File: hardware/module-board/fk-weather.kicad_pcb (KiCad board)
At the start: 2 copper layers, 37.5 x 103 mm, 72 parts, among them J1 MICRO-USB, J10 CONN_01x06, J11 CONN_01x06, J2 CONN_01x05, J3 CONN_01x03_SERIAL, J4 CONN_01x04, J5 Conn_01x02, J6 CONN_02x05_SWD, J7 CONN_01x05, Q4 2N7002LT1G, SW1 SPNO, U1 ATSAMD21G18A-AU, U2 MCP1700T-3302E/MB, U3 TPS2051B, U4 S25FL116K0XMFI041, U5 SK6812, U6 PCF8523, Y1 FC-135, Y2 FC-135

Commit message: Adding some pull downs.
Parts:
- added R3: ?, conservify:RES-0603, F.Cu at (94.0, 143.4)
- added R5: ?, conservify:RES-0603, F.Cu at (88.4, 146.2)
- J5: value Conn_01x02 -> CONN_01x02
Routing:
- net /D8_PERIPH_EN: track 27.7 -> 30.4 mm, vias 2 -> 3
- net /PERIPH_3V3: track 24.3 -> 26.2 mm
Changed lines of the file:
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@@
-(kicad_pcb (version 20171130) (host pcbnew 5.0.0-fee4fd1~66~ubuntu16.04.1)
+(kicad_pcb (version 20171130) (host pcbnew 5.0.1-33cea8e~67~ubuntu18.04.1)
   (general
     (thickness 1.6)
     (drawings 16)
-    (tracks 709)
+    (tracks 715)
     (zones 0)
-    (modules 72)
+    (modules 74)
     (nets 80)
   )
@@
     (pad_drill 0)
     (pad_to_mask_clearance 0.1016)
+    (solder_mask_min_width 0.25)
     (pad_to_paste_clearance_ratio -0.05)
     (aux_axis_origin 127 127)
@@
       (effects (font (size 0.8 0.8) (thickness 0.12)))
     )
-    (fp_text value Conn_01x02 (at 0 1.6 90) (layer Eco1.User) hide
+    (fp_text value CONN_01x02 (at 0 1.6 90) (layer Eco1.User) hide
       (effects (font (size 0.6 0.6) (thickness 0.1)))
     )
@@
     (pad "" np_thru_hole circle (at -6 0 270) (size 2.36 2.36) (drill 2.36) (layers *.Cu *.Mask F.SilkS))
   )
+  (module conservify:RES-0603 (layer F.Cu)
+    (at 93.98 143.383 180)
+    (descr "Capacitor SMD 0603")
+    (tags "capacitor 0603")
+    (attr smd)
+    (fp_text reference R3 (at 0 -1.5748 180) (layer F.SilkS) hide
+      (effects (font (size 1 1) (thickness 0.15)))
+    )
+    (fp_text value ? (at 0 1.9 180) (layer F.Fab)
+      (effects (font (size 1 1) (thickness 0.15)))
+    )
+    (fp_line (start -1.65 -0.75) (end -1.65 0.75) (layer F.CrtYd) (width 0.05))
+    (fp_line (start -1.65 0.75) (end 1.65 0.75) (layer F.CrtYd) (width 0.05))
+    (fp_line (start 1.65 0.75) (end 1.65 -0.75) (layer F.CrtYd) (width 0.05))
+    (fp_line (start 1.65 -0.75) (end -1.65 -0.75) (layer F.CrtYd) (width 0.05))
+    (fp_line (start -1.6 -0.7) (end -1.6 0.7) (layer F.SilkS) (width 0.15))
+    (fp_line (start 1.6 -0.7) (end 1.6 0.7) (layer F.SilkS) (width 0.15))
+    (fp_line (start -1.6 -0.7) (end 1.6 -0.7) (layer F.SilkS) (width 0.15))
+    (fp_line (start 1.6 0.7) (end -1.6 0.7) (layer F.SilkS) (width 0.15))
+    (pad 1 smd rect (at -0.85 0 180) (size 1.1 1) (layers F.Cu F.Paste F.Mask)
+      (net 1 GND))
+    (pad 2 smd rect (at 0.85 0 180) (size 1.1 1) (layers F.Cu F.Paste F.Mask)
+      (net 76 /D8_PERIPH_EN))
+  )
+  (module conservify:RES-0603 (layer F.Cu)
+    (at 88.392 146.177)
+    (descr "Capacitor SMD 0603")
+    (tags "capacitor 0603")
+    (attr smd)
+    (fp_text reference R5 (at 0 -1.5748) (layer F.SilkS) hide
+      (effects (font (size 1 1) (thickness 0.15)))
+    )
+    (fp_text value ? (at 0 1.9) (layer F.Fab)
+      (effects (font (size 1 1) (thickness 0.15)))
+    )
+    (fp_line (start 1.6 0.7) (end -1.6 0.7) (layer F.SilkS) (width 0.15))
+    (fp_line (start -1.6 -0.7) (end 1.6 -0.7) (layer F.SilkS) (width 0.15))
+    (fp_line (start 1.6 -0.7) (end 1.6 0.7) (layer F.SilkS) (width 0.15))
+    (fp_line (start -1.6 -0.7) (end -1.6 0.7) (layer F.SilkS) (width 0.15))
+    (fp_line (start 1.65 -0.75) (end -1.65 -0.75) (layer F.CrtYd) (width 0.05))
+    (fp_line (start 1.65 0.75) (end 1.65 -0.75) (layer F.CrtYd) (width 0.05))
+    (fp_line (start -1.65 0.75) (end 1.65 0.75) (layer F.CrtYd) (width 0.05))
+    (fp_line (start -1.65 -0.75) (end -1.65 0.75) (layer F.CrtYd) (width 0.05))
+    (pad 2 smd rect (at 0.85 0) (size 1.1 1) (layers F.Cu F.Paste F.Mask)
+      (net 65 /PERIPH_3V3))
+    (pad 1 smd rect (at -0.85 0) (size 1.1 1) (layers F.Cu F.Paste F.Mask)
+      (net 1 GND))
+  )
   (gr_text SERIAL (at 113.792 159.131 90) (layer F.SilkS)
     (effects (font (size 0.8 0.8) (thickness 0.2)))
@@
   (segment (start 94.471414 148.1963) (end 94.0834 148.1963) (width 0.254) (layer F.Cu) (net 65))
   (segment (start 94.0834 148.1963) (end 92.8294 148.1963) (width 0.254) (layer F.Cu) (net 65))
-  (segment (start 87.5783 147.6765) (end 87.4649 147.7899) (width 0.254) (layer F.Cu) (net 65))
   (segment (start 89.4461 148.1845) (end 87.5783 148.1845) (width 0.254) (layer F.Cu) (net 65))
   (segment (start 92.3176 148.1845) (end 92.3294 148.1963) (width 0.254) (layer F.Cu) (net 65))
   (segment (start 89.4461 148.1845) (end 92.3176 148.1845) (width 0.254) (layer F.Cu) (net 65))
+  (segment (start 89.4461 146.3811) (end 89.242 146.177) (width 0.254) (layer F.Cu) (net 65))
+  (segment (start 89.4461 148.1845) (end 89.4461 146.3811) (width 0.254) (layer F.Cu) (net 65))
   (segment (start 90.814917 139.483979) (end 90.814917 138.422) (width 0.254) (layer F.Cu) (net 66))
   (segment (start 90.814917 138.422) (end 89.806917 137.414) (width 0.254) (layer F.Cu) (net 66))
@@
   (segment (start 92.410919 160.2613) (end 90.5764 160.2613) (width 0.254) (layer F.Cu) (net 76))
   (via (at 90.5764 160.2613) (size 0.5) (drill 0.3) (layers F.Cu B.Cu) (net 76))
+  (segment (start 90.5637 160.274) (end 90.5764 160.2613) (width 0.254) (layer F.Cu) (net 76))
+  (via (at 91.821 143.383) (size 0.5) (drill 0.3) (layers F.Cu B.Cu) (net 76))
+  (segment (start 93.13 143.383) (end 91.821 143.383) (width 0.254) (layer F.Cu) (net 76))
+  (segment (start 90.955353 143.383) (end 90.5764 143.761953) (width 0.254) (layer B.Cu) (net 76))
+  (segment (start 91.821 143.383) (end 90.955353 143.383) (width 0.254) (layer B.Cu) (net 76))
   (segment (start 97.5614 165.9128) (end 97.976358 166.327758) (width 0.254) (layer F.Cu) (net 77))
   (segment (start 97.976358 166.327758) (end 97.976358 167.735929) (width 0.254) (layer F.Cu) (net 77))
@@
     (connect_pads (clearance 0.2032))
     (min_thickness 0.253)
-    (fill (arc_segments 32) (thermal_gap 0.254) (thermal_bridge_width 0.254) (smoothing chamfer))
+    (fill yes (arc_segments 32) (thermal_gap 0.254) (thermal_bridge_width 0.254) (smoothing chamfer))
     (polygon
       (pts
@@
     (connect_pads (clearance 0.2032))
     (min_thickness 0.253)
-    (fill (arc_segments 32) (thermal_gap 0.254) (thermal_bridge_width 0.254) (smoothing chamfer))
+    (fill yes (arc_segments 32) (thermal_gap 0.254) (thermal_bridge_width 0.254) (smoothing chamfer))
     (polygon
       (pts
@@
     (connect_pads (clearance 0.2032))
     (min_thickness 0.253)
-    (fill (arc_segments 32) (thermal_gap 0.254) (thermal_bridge_width 0.254) (smoothing chamfer))
+    (fill yes (arc_segments 32) (thermal_gap 0.254) (thermal_bridge_width 0.254) (smoothing chamfer))
     (polygon
       (pts
@@
     (connect_pads (clearance 0.2032))
     (min_thickness 0.253)
-    (fill (arc_segments 32) (thermal_gap 0.254) (thermal_bridge_width 0.254) (smoothing chamfer))
+    (fill yes (arc_segments 32) (thermal_gap 0.254) (thermal_bridge_width 0.254) (smoothing chamfer))
     (polygon
       (pts

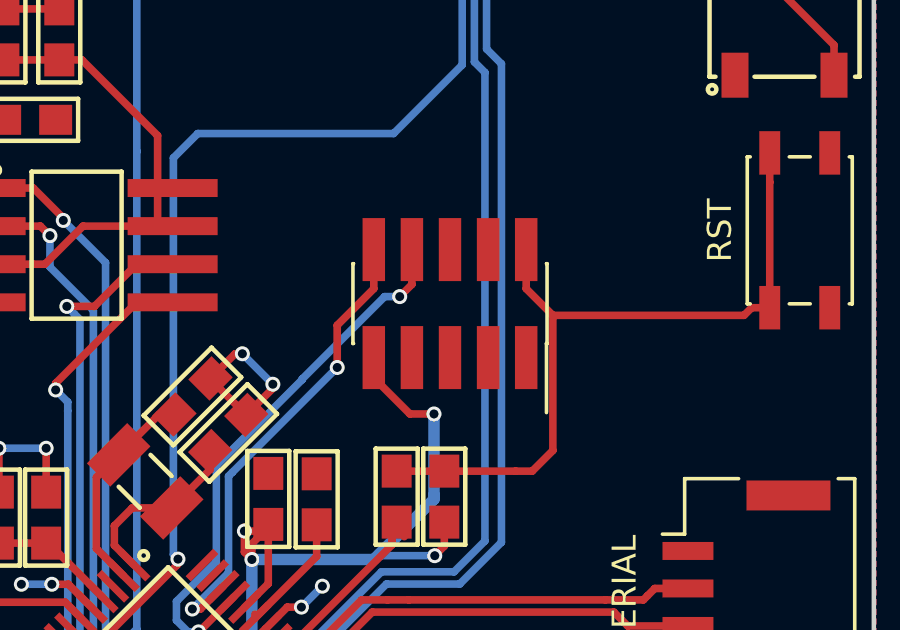
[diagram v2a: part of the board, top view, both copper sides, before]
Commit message: Add orientation indicator to SWD fp.
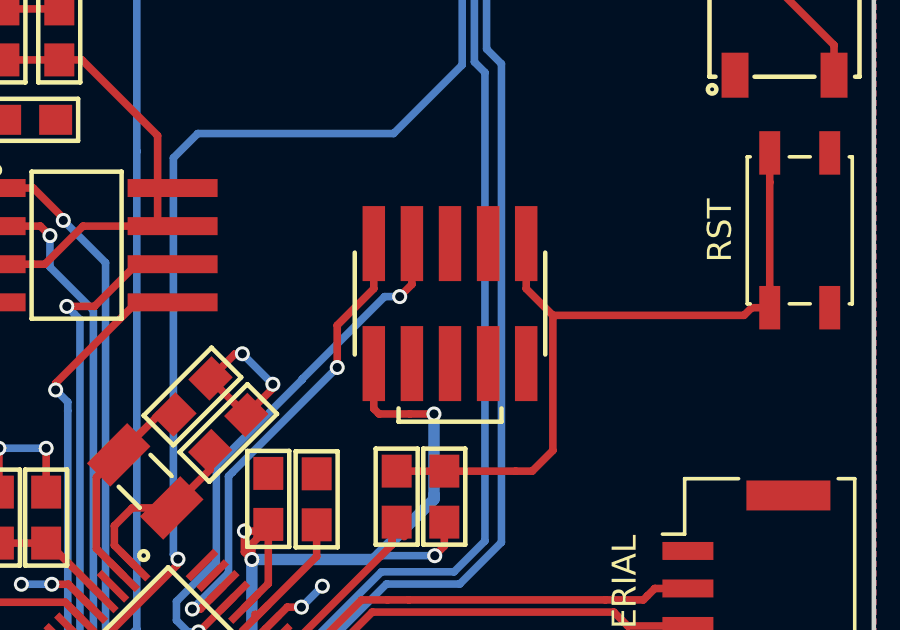
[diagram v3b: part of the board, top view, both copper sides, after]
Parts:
- turned J6 to 0 degrees
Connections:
- J6 pad 1: GND -> 3V3
- J6 pad 10: /SWDIO -> /RST
- J6 pad 2: /RST -> /SWDIO
- J6 pad 3: Net-(J6-Pad3) -> GND
- J6 pad 4: Net-(J6-Pad4) -> /SWCLK
- J6 pad 7: GND -> Net-(J6-Pad7)
- J6 pad 8: /SWCLK -> Net-(J6-Pad8)
- J6 pad 9: 3V3 -> GND
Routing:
- net 3V3: track 290.4 -> 291.5 mm

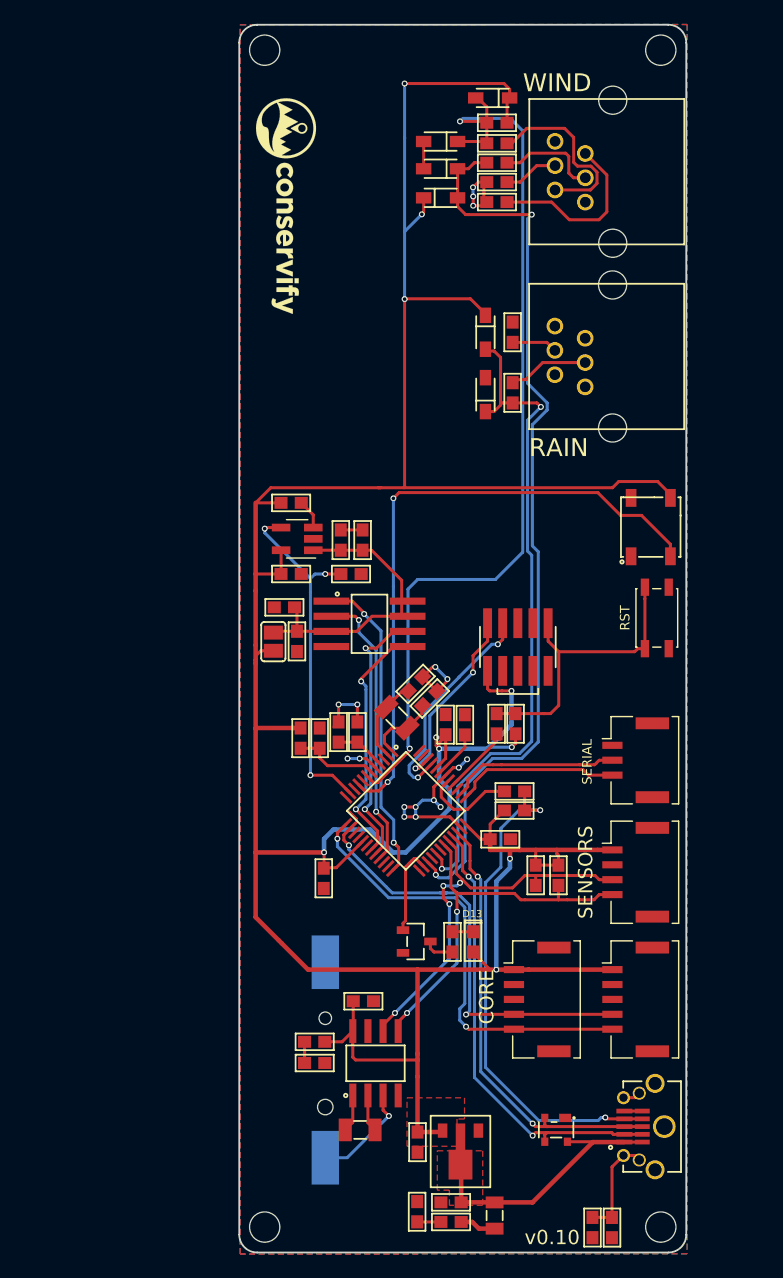
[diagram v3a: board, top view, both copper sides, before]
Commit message: Switch to 2.7mm mounting holes.
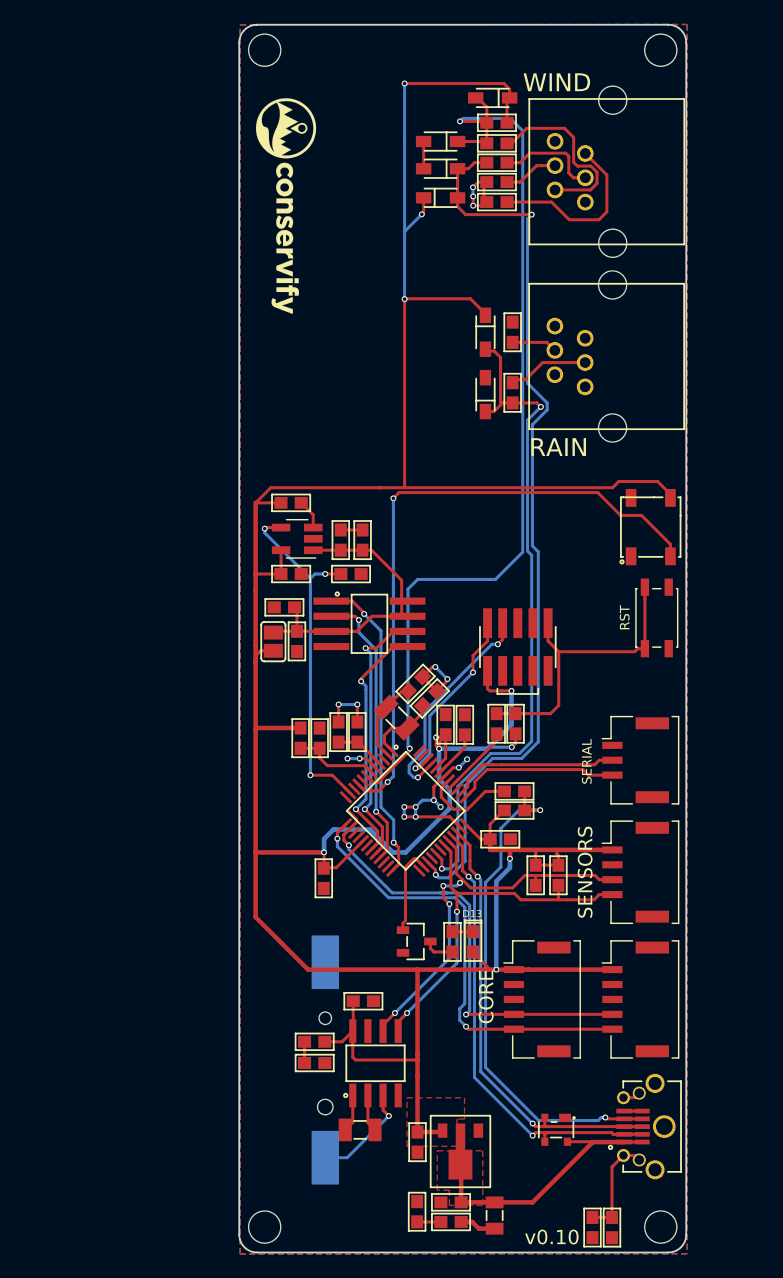
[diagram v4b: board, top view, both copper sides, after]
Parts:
- removed REF** (x4): HOLE_NPTH_2.54MM, conservify:HOLE_NPTH_2.54MM
- added M1: MOUNT_HOLE, conservify:HOLE_NPTH_2.7MM, F.Cu at (86.7, 99.4)
- added M2: MOUNT_HOLE, conservify:HOLE_NPTH_2.7MM, F.Cu at (86.7, 198.2)
- added M3: MOUNT_HOLE, conservify:HOLE_NPTH_2.7MM, F.Cu at (120.0, 198.2)
- added M4: MOUNT_HOLE, conservify:HOLE_NPTH_2.7MM, F.Cu at (120.0, 99.4)
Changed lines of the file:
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@@
     )
-  )
-  (module conservify:HOLE_NPTH_2.54MM (layer F.Cu)
-    (at 86.738445 99.437083 90)
-    (fp_text reference REF** (at 0 -2.54 90) (layer F.SilkS) hide
-      (effects (font (size 1 1) (thickness 0.15)))
-    )
-    (fp_text value HOLE_NPTH_2.54MM (at 0 2.54 90) (layer F.Fab) hide
-      (effects (font (size 1 1) (thickness 0.15)))
-    )
-    (pad "" np_thru_hole circle (at 0 0 90) (size 2.54 2.54) (drill 2.54) (layers *.Cu *.Mask F.SilkS))
-  )
-  (module conservify:HOLE_NPTH_2.54MM (layer F.Cu)
-    (at 86.738445 198.167083 90)
-    (fp_text reference REF** (at 0 -2.54 90) (layer F.SilkS) hide
-      (effects (font (size 1 1) (thickness 0.15)))
-    )
-    (fp_text value HOLE_NPTH_2.54MM (at 0 2.54 90) (layer F.Fab) hide
-      (effects (font (size 1 1) (thickness 0.15)))
-    )
-    (pad "" np_thru_hole circle (at 0 0 90) (size 2.54 2.54) (drill 2.54) (layers *.Cu *.Mask F.SilkS))
-  )
-  (module conservify:HOLE_NPTH_2.54MM (layer F.Cu)
-    (at 119.968445 198.167083 90)
-    (fp_text reference REF** (at 0 -2.54 90) (layer F.SilkS) hide
-      (effects (font (size 1 1) (thickness 0.15)))
-    )
-    (fp_text value HOLE_NPTH_2.54MM (at 0 2.54 90) (layer F.Fab) hide
-      (effects (font (size 1 1) (thickness 0.15)))
-    )
-    (pad "" np_thru_hole circle (at 0 0 90) (size 2.54 2.54) (drill 2.54) (layers *.Cu *.Mask F.SilkS))
-  )
-  (module conservify:HOLE_NPTH_2.54MM (layer F.Cu)
-    (at 119.968445 99.437083 90)
-    (fp_text reference REF** (at 0 -2.54 90) (layer F.SilkS) hide
-      (effects (font (size 1 1) (thickness 0.15)))
-    )
-    (fp_text value HOLE_NPTH_2.54MM (at 0 2.54 90) (layer F.Fab) hide
-      (effects (font (size 1 1) (thickness 0.15)))
-    )
-    (pad "" np_thru_hole circle (at 0 0 90) (size 2.54 2.54) (drill 2.54) (layers *.Cu *.Mask F.SilkS))
   )
   (module conservify:SK6812 (layer F.Cu)
@@
       (net 1 GND))
   )
+  (module conservify:HOLE_NPTH_2.7MM (layer F.Cu)
+    (at 86.738445 99.437083 90)
+    (fp_text reference M1 (at 0 -2.54 90) (layer F.SilkS) hide
+      (effects (font (size 1 1) (thickness 0.15)))
+    )
+    (fp_text value MOUNT_HOLE (at 0 2.54 90) (layer F.Fab)
+      (effects (font (size 1 1) (thickness 0.15)))
+    )
+    (pad "" np_thru_hole circle (at 0 0 90) (size 2.7 2.7) (drill 2.7) (layers *.Cu *.Mask F.SilkS))
+  )
+  (module conservify:HOLE_NPTH_2.7MM (layer F.Cu)
+    (at 86.738445 198.167083 90)
+    (fp_text reference M2 (at 0 -2.54 90) (layer F.SilkS) hide
+      (effects (font (size 1 1) (thickness 0.15)))
+    )
+    (fp_text value MOUNT_HOLE (at 0 2.54 90) (layer F.Fab)
+      (effects (font (size 1 1) (thickness 0.15)))
+    )
+    (pad "" np_thru_hole circle (at 0 0 90) (size 2.7 2.7) (drill 2.7) (layers *.Cu *.Mask F.SilkS))
+  )
+  (module conservify:HOLE_NPTH_2.7MM (layer F.Cu)
+    (at 119.968445 198.167083 90)
+    (fp_text reference M3 (at 0 -2.54 90) (layer F.SilkS) hide
+      (effects (font (size 1 1) (thickness 0.15)))
+    )
+    (fp_text value MOUNT_HOLE (at 0 2.54 90) (layer F.Fab)
+      (effects (font (size 1 1) (thickness 0.15)))
+    )
+    (pad "" np_thru_hole circle (at 0 0 90) (size 2.7 2.7) (drill 2.7) (layers *.Cu *.Mask F.SilkS))
+  )
+  (module conservify:HOLE_NPTH_2.7MM (layer F.Cu)
+    (at 119.968445 99.437083 90)
+    (fp_text reference M4 (at 0 -2.54 90) (layer F.SilkS) hide
+      (effects (font (size 1 1) (thickness 0.15)))
+    )
+    (fp_text value MOUNT_HOLE (at 0 2.54 90) (layer F.Fab)
+      (effects (font (size 1 1) (thickness 0.15)))
+    )
+    (pad "" np_thru_hole circle (at 0 0 90) (size 2.7 2.7) (drill 2.7) (layers *.Cu *.Mask F.SilkS))
+  )
   (gr_text SERIAL (at 113.792 159.131 90) (layer F.SilkS)

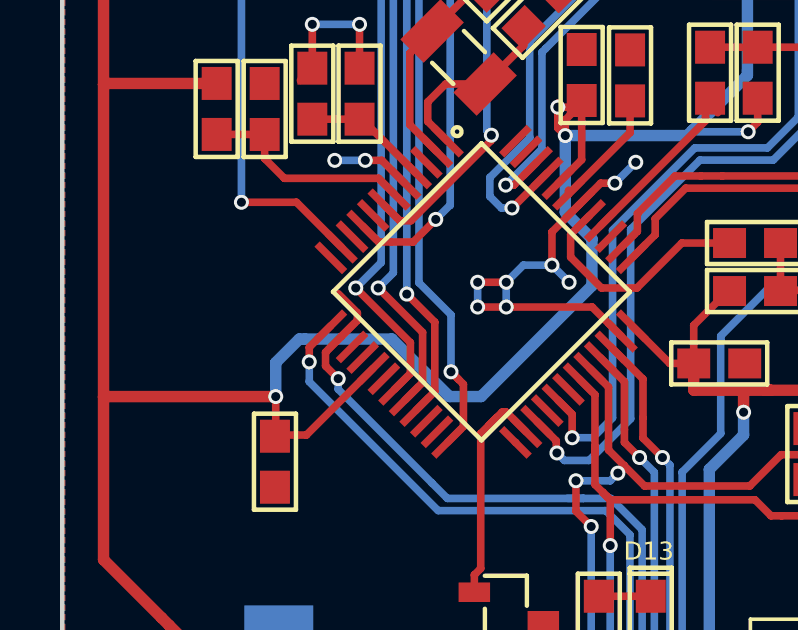
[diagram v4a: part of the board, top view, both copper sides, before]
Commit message: Remove extra trace.
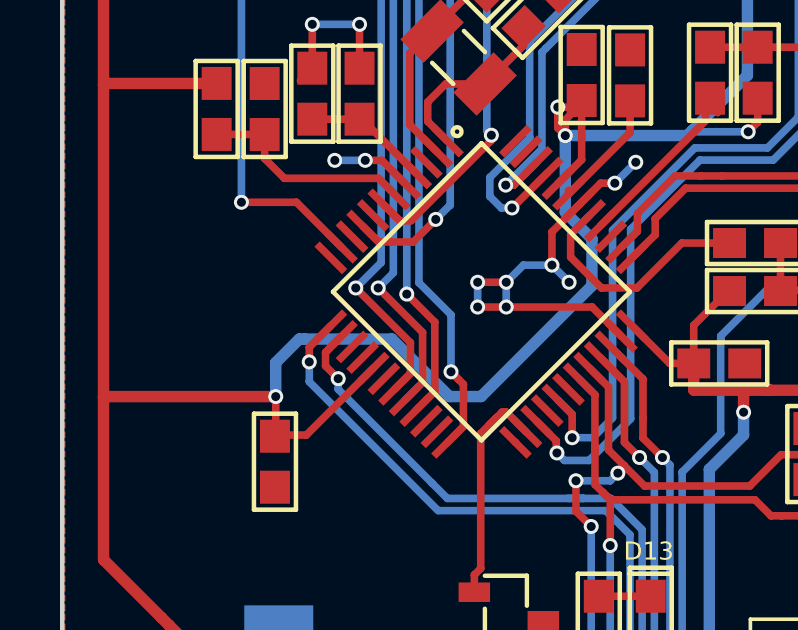
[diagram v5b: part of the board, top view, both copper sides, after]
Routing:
- net /SCL2: track 38.3 -> 36.4 mm
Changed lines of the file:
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@@
     (thickness 1.6)
     (drawings 16)
-    (tracks 717)
+    (tracks 714)
     (zones 0)
     (modules 74)
@@
   (segment (start 93.380166 165.719366) (end 93.8022 166.1414) (width 0.254) (layer F.Cu) (net 58))
   (via (at 93.8022 166.1414) (size 0.5) (drill 0.3) (layers F.Cu B.Cu) (net 58))
-  (segment (start 94.440824 164.200395) (end 93.910495 164.730724) (width 0.254) (layer F.Cu) (net 58))
-  (segment (start 93.8022 163.308043) (end 94.440824 163.946667) (width 0.254) (layer F.Cu) (net 58))
-  (segment (start 94.440824 163.946667) (end 94.440824 164.200395) (width 0.254) (layer F.Cu) (net 58))
   (segment (start 107.651 181.57) (end 103.846 181.57) (width 0.254) (layer F.Cu) (net 59))
   (segment (start 103.846 181.57) (end 103.632 181.356) (width 0.254) (layer F.Cu) (net 59))
